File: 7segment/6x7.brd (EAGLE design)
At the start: 78.4 x 49.5 mm, 22 parts, among them IC1 AT90S2313P, IC2 7805TV

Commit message: 7segment 6x7: Add LED resistor values
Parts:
- R10, R11, R4, R5, R6, R7, R8, R9: value (none) -> 470
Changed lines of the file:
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@@
 <attribute name="VALUE" x="52.197" y="26.6192" size="1.27" layer="27" ratio="10"/>
 </element>
-<element name="R4" library="rcl" package="0207/10" value="" x="53.34" y="19.05" smashed="yes" rot="R90">
+<element name="R4" library="rcl" package="0207/10" value="470" x="53.34" y="19.05" smashed="yes" rot="R90">
 <attribute name="NAME" x="52.197" y="25.019" size="1.27" layer="25" ratio="10"/>
 <attribute name="VALUE" x="53.975" y="16.7894" size="1.27" layer="27" ratio="10" rot="R90"/>
 </element>
-<element name="R5" library="rcl" package="0207/10" value="" x="55.88" y="19.05" smashed="yes" rot="R90">
+<element name="R5" library="rcl" package="0207/10" value="470" x="55.88" y="19.05" smashed="yes" rot="R90">
 <attribute name="NAME" x="54.737" y="25.019" size="1.27" layer="25" ratio="10"/>
 <attribute name="VALUE" x="56.515" y="16.7894" size="1.27" layer="27" ratio="10" rot="R90"/>
 </element>
-<element name="R6" library="rcl" package="0207/10" value="" x="58.42" y="19.05" smashed="yes" rot="R90">
+<element name="R6" library="rcl" package="0207/10" value="470" x="58.42" y="19.05" smashed="yes" rot="R90">
 <attribute name="NAME" x="57.277" y="25.019" size="1.27" layer="25" ratio="10"/>
 <attribute name="VALUE" x="59.055" y="16.7894" size="1.27" layer="27" ratio="10" rot="R90"/>
 </element>
-<element name="R7" library="rcl" package="0207/10" value="" x="60.96" y="19.05" smashed="yes" rot="R90">
+<element name="R7" library="rcl" package="0207/10" value="470" x="60.96" y="19.05" smashed="yes" rot="R90">
 <attribute name="NAME" x="59.817" y="25.019" size="1.27" layer="25" ratio="10"/>
 <attribute name="VALUE" x="61.595" y="16.7894" size="1.27" layer="27" ratio="10" rot="R90"/>
 </element>
-<element name="R8" library="rcl" package="0207/10" value="" x="63.5" y="19.05" smashed="yes" rot="R90">
+<element name="R8" library="rcl" package="0207/10" value="470" x="63.5" y="19.05" smashed="yes" rot="R90">
 <attribute name="NAME" x="62.357" y="25.019" size="1.27" layer="25" ratio="10"/>
 <attribute name="VALUE" x="64.135" y="16.7894" size="1.27" layer="27" ratio="10" rot="R90"/>
 </element>
-<element name="R9" library="rcl" package="0207/10" value="" x="66.04" y="19.05" smashed="yes" rot="R90">
+<element name="R9" library="rcl" package="0207/10" value="470" x="66.04" y="19.05" smashed="yes" rot="R90">
 <attribute name="NAME" x="64.897" y="25.019" size="1.27" layer="25" ratio="10"/>
 <attribute name="VALUE" x="66.675" y="16.7894" size="1.27" layer="27" ratio="10" rot="R90"/>
 </element>
-<element name="R10" library="rcl" package="0207/10" value="" x="68.58" y="19.05" smashed="yes" rot="R90">
+<element name="R10" library="rcl" package="0207/10" value="470" x="68.58" y="19.05" smashed="yes" rot="R90">
 <attribute name="NAME" x="67.437" y="25.019" size="1.27" layer="25" ratio="10"/>
 <attribute name="VALUE" x="69.215" y="16.7894" size="1.27" layer="27" ratio="10" rot="R90"/>
 </element>
-<element name="R11" library="rcl" package="0207/10" value="" x="71.12" y="19.05" smashed="yes" rot="R90">
+<element name="R11" library="rcl" package="0207/10" value="470" x="71.12" y="19.05" smashed="yes" rot="R90">
 <attribute name="NAME" x="71.247" y="25.019" size="1.27" layer="25" ratio="10"/>
 <attribute name="VALUE" x="71.755" y="16.7894" size="1.27" layer="27" ratio="10" rot="R90"/>

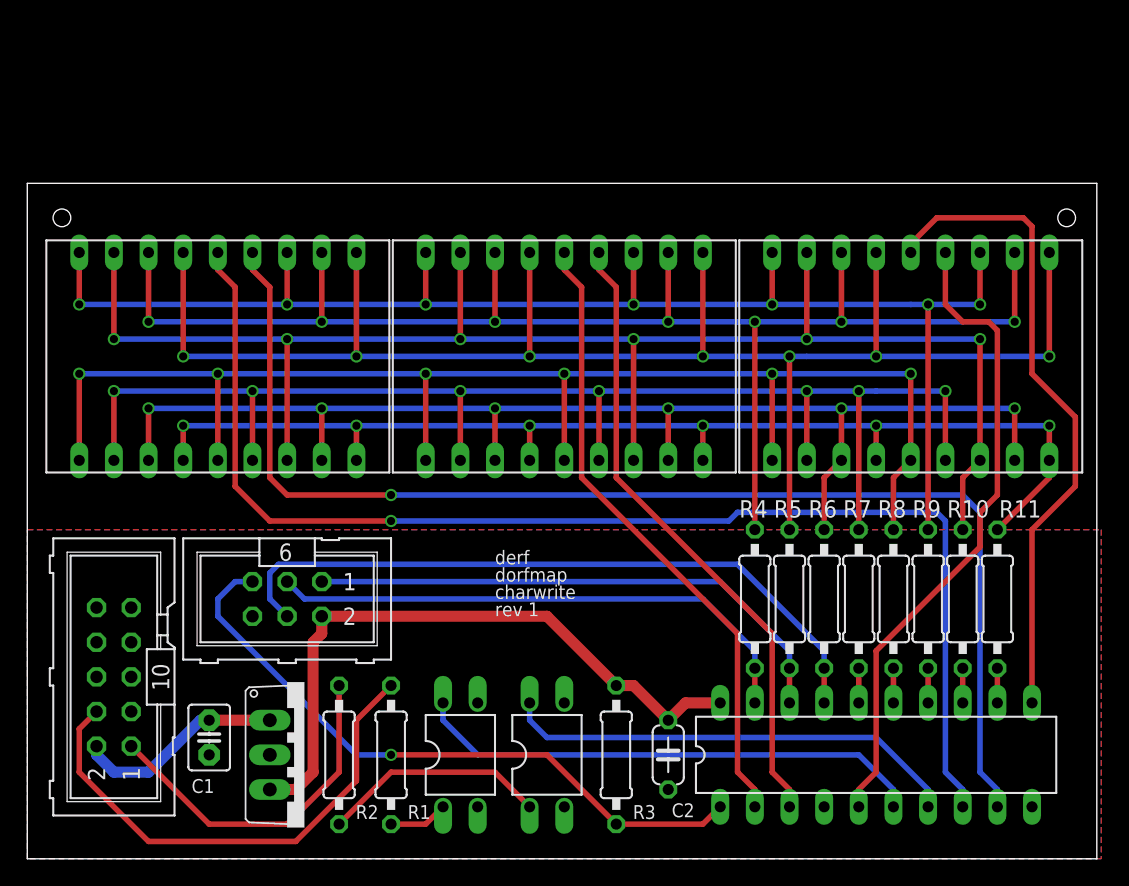
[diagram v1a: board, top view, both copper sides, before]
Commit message: 7segment: re-order parts for nicer(?) layout. TODO: routing
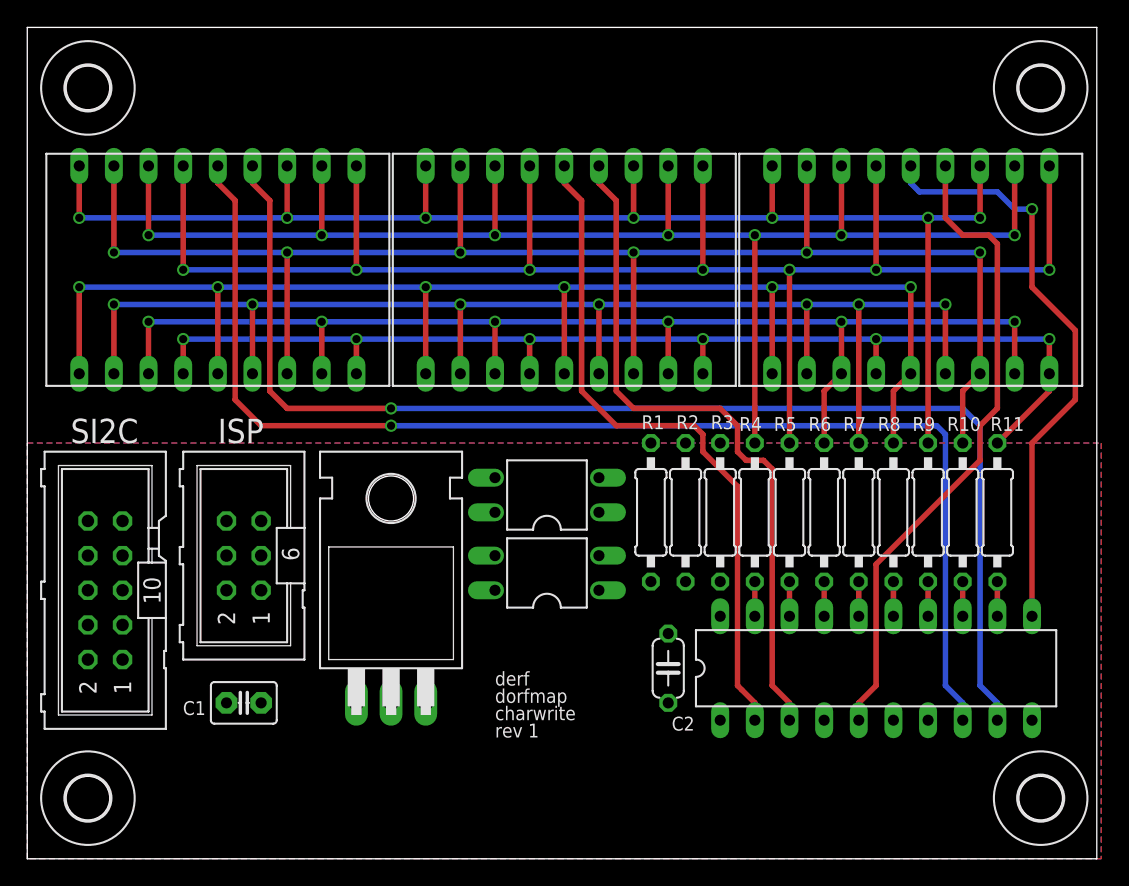
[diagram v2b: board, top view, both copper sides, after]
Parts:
- added H1, H2, H3, H4: MOUNT-HOLE3.2, holes:3,2
- IC2: value 7805TV -> 7805T; device linear:TO220V -> linear:TO220H
- SV2: value (none) -> ISP
- moved R2 31.0 mm to (48.3, 25.4)
- moved R1 26.1 mm to (45.7, 25.4)
- moved R3 19.3 mm to (50.8, 25.4)
- moved OK2 19.1 mm to (38.1, 26.7), turned to 90 degrees
- moved IC2 15.3 mm to (26.7, 21.6), turned to 0 degrees
- moved OK1 14.8 mm to (38.1, 21.0), turned to 90 degrees
- moved SV1 6.38 mm to (5.71, 19.7)
- moved DIS1 6.35 mm to (14.0, 43.2)
- moved DIS2 6.35 mm to (39.4, 43.2)
- moved DIS3 6.35 mm to (64.8, 43.2)
- moved C2 6.35 mm to (47.0, 14.0)
- moved IC1 6.35 mm to (62.2, 14.0)
- moved R10 6.35 mm to (68.6, 25.4)
- moved R11 6.35 mm to (71.1, 25.4)
- moved R4 6.35 mm to (53.3, 25.4)
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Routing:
- net N$7: track 51.0 -> 2.54 mm
- net 5V: track 48.3 -> 0.00 mm
- net N$3: track 48.0 -> 0.00 mm, vias 1 -> 0
- net N$5: track 40.2 -> 2.54 mm
- net N$2: track 40.2 -> 2.54 mm
- net AVRSCL: track 37.7 -> 0.00 mm
- net SCL: track 37.3 -> 0.00 mm
- net AVRSDA: track 33.9 -> 0.00 mm
- net SDA: track 25.5 -> 0.00 mm
- net N$4: track 16.6 -> 0.00 mm
- net VCC: track 15.4 -> 0.00 mm
- net D4: track 48.8 -> 43.4 mm, vias 0 -> 1
- net D1: track 46.4 -> 50.9 mm
- net N$1: track 4.34 -> 0.00 mm
- net D0: track 46.4 -> 49.8 mm
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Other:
- board size 78.4 x 49.5 mm -> 78.4 x 61 mm
- board text added: "ISP"
- board text added: "SI2C"

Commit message: 7segment/6x7: YOLO Routing Co. reporting in.
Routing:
- net 5V: track 0.00 -> 58.0 mm, vias 0 -> 1
- net N$7: track 2.54 -> 57.8 mm
- net SDA: track 0.00 -> 54.2 mm
- net SCL: track 0.00 -> 52.0 mm
- net N$3: track 0.00 -> 51.9 mm
- net N$2: track 2.54 -> 48.4 mm
- net N$5: track 2.54 -> 44.9 mm, vias 0 -> 1
- net AVRSDA: track 0.00 -> 39.6 mm
- net AVRSCL: track 0.00 -> 33.9 mm
- net VCC: track 0.00 -> 24.2 mm
- net N$4: track 0.00 -> 10.7 mm
- net N$1: track 0.00 -> 4.07 mm
- net D1: track 50.9 -> 51.9 mm
- net D0: track 49.8 -> 50.8 mm

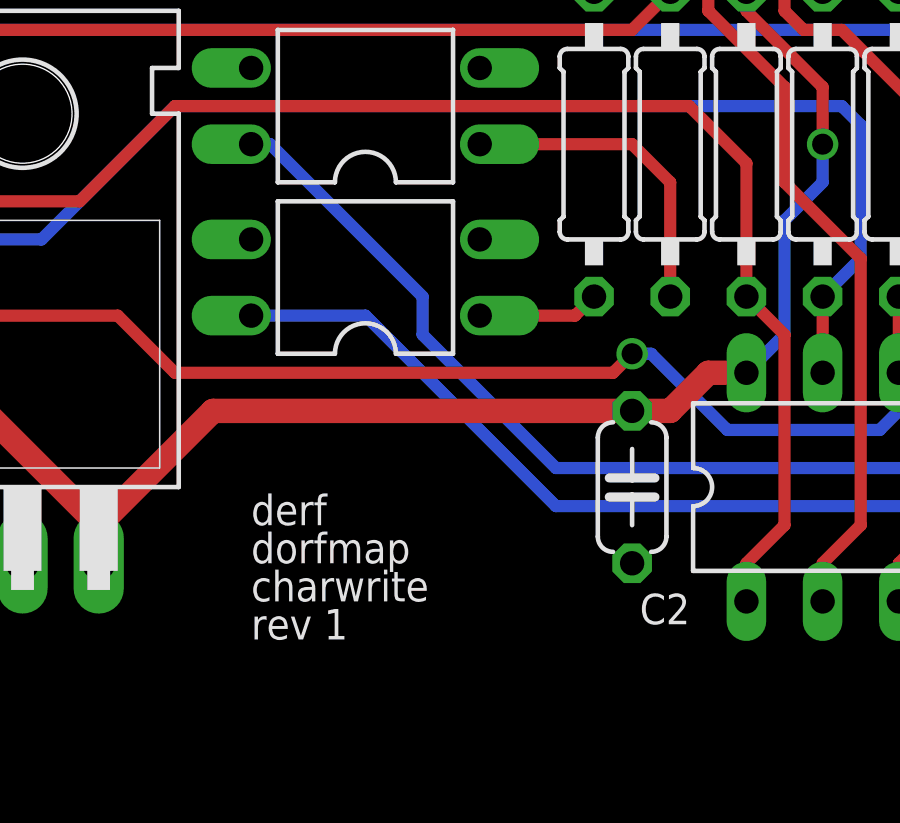
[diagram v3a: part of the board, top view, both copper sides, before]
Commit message: 7segment/6x7: Position 2xPC817 to allow 1xPC827 as drop-in replacement
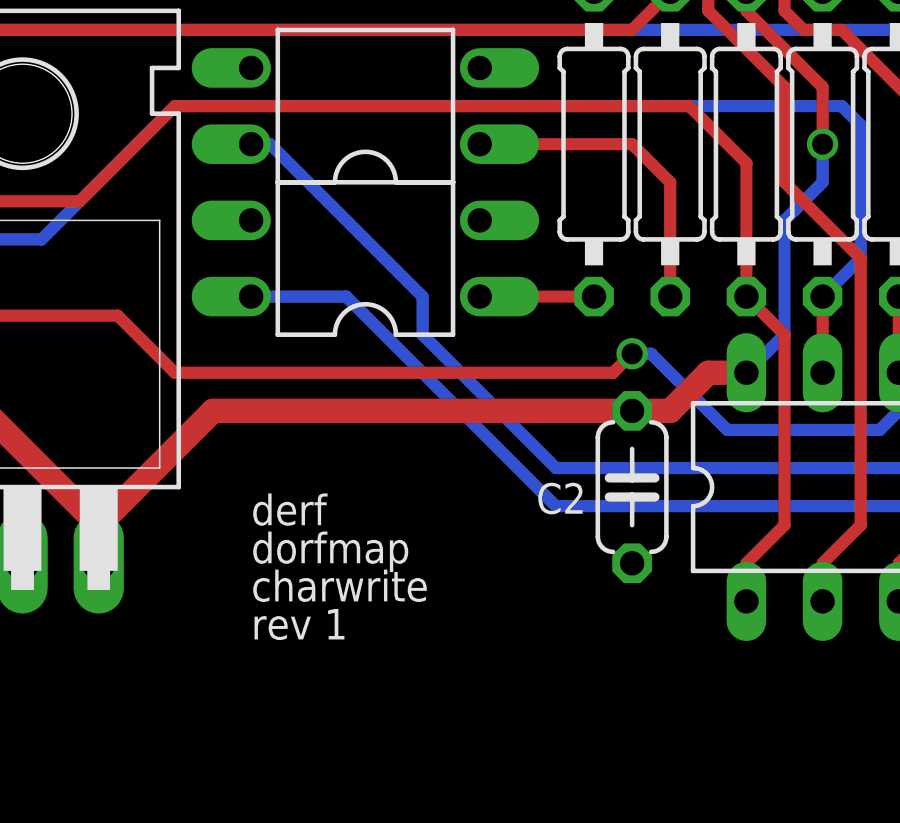
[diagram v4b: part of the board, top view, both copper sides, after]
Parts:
- moved OK1 0.64 mm to (38.1, 21.6)
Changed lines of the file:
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@@
 <attribute name="VALUE" x="52.07" y="13.208" size="1.778" layer="27" ratio="10"/>
 </element>
-<element name="OK1" library="optocoupler" package="DIL04" value="PC817" x="38.1" y="20.955" smashed="yes" rot="R90">
-<attribute name="OC_NEWARK" value="97K7059" x="45.72" y="38.735" size="1.778" layer="27" rot="R90" display="off"/>
-<attribute name="MPN" value="PC817X4J000F" x="45.72" y="38.735" size="1.778" layer="27" rot="R90" display="off"/>
-<attribute name="MF" value="" x="45.72" y="38.735" size="1.778" layer="27" rot="R90" display="off"/>
-<attribute name="OC_FARNELL" value="9707727" x="45.72" y="38.735" size="1.778" layer="27" rot="R90" display="off"/>
-<attribute name="VALUE" x="41.021" y="25.146" size="1.27" layer="27" ratio="10" rot="R180"/>
-<attribute name="NAME" x="39.751" y="22.352" size="1.27" layer="27" ratio="10" rot="R270"/>
+<element name="OK1" library="optocoupler" package="DIL04" value="PC817" x="38.1" y="21.59" smashed="yes" rot="R90">
+<attribute name="OC_NEWARK" value="97K7059" x="45.72" y="39.37" size="1.778" layer="27" rot="R90" display="off"/>
+<attribute name="MPN" value="PC817X4J000F" x="45.72" y="39.37" size="1.778" layer="27" rot="R90" display="off"/>
+<attribute name="MF" value="" x="45.72" y="39.37" size="1.778" layer="27" rot="R90" display="off"/>
+<attribute name="OC_FARNELL" value="9707727" x="45.72" y="39.37" size="1.778" layer="27" rot="R90" display="off"/>
+<attribute name="VALUE" x="41.021" y="25.781" size="1.27" layer="27" ratio="10" rot="R180"/>
+<attribute name="NAME" x="39.751" y="22.987" size="1.27" layer="27" ratio="10" rot="R270"/>
 </element>
 <element name="OK2" library="optocoupler" package="DIL04" value="PC817" x="38.1" y="26.67" smashed="yes" rot="R90">
@@
 </element>
 <element name="C2" library="rcl" package="C050-024X044" value="100nF" x="46.99" y="13.97" smashed="yes" rot="R270">
-<attribute name="NAME" x="47.244" y="9.398" size="1.016" layer="25" font="vector" ratio="10"/>
+<attribute name="NAME" x="45.466" y="14.097" size="1.016" layer="25" font="vector" ratio="10" rot="R180"/>
 <attribute name="VALUE" x="43.942" y="15.621" size="1.27" layer="27" ratio="10" rot="R270"/>
 </element>
@@
 <contactref element="OK1" pad="4"/>
 <contactref element="IC1" pad="6"/>
-<wire x1="34.29" y1="19.685" x2="38.1" y2="19.685" width="0.4064" layer="16"/>
-<wire x1="38.1" y1="19.685" x2="44.45" y2="13.335" width="0.4064" layer="16"/>
+<wire x1="34.29" y1="20.32" x2="37.465" y2="20.32" width="0.4064" layer="16"/>
+<wire x1="37.465" y1="20.32" x2="44.45" y2="13.335" width="0.4064" layer="16"/>
 <wire x1="44.45" y1="13.335" x2="61.595" y2="13.335" width="0.4064" layer="16"/>
 <wire x1="61.595" y1="13.335" x2="63.5" y2="11.43" width="0.4064" layer="16"/>
@@
 <contactref element="OK1" pad="1"/>
 <contactref element="R1" pad="2"/>
-<wire x1="45.72" y1="20.32" x2="45.085" y2="19.685" width="0.4064" layer="1"/>
-<wire x1="45.085" y1="19.685" x2="41.91" y2="19.685" width="0.4064" layer="1"/>
+<wire x1="45.72" y1="20.32" x2="41.91" y2="20.32" width="0.4064" layer="1"/>
 </signal>
 <signal name="VCC">
